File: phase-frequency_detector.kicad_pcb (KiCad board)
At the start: 2 copper layers, 160 x 100 mm, 89 parts, among them J1 REF, J2 IN, J3 Error_Out, J4 C64AC, J5 Switch, J6 Fast_Out, U1 HMC439QS16G, U2 LT3045EMSE, U3 LT3094EMSE, U4 ADA4896-2ARMZ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

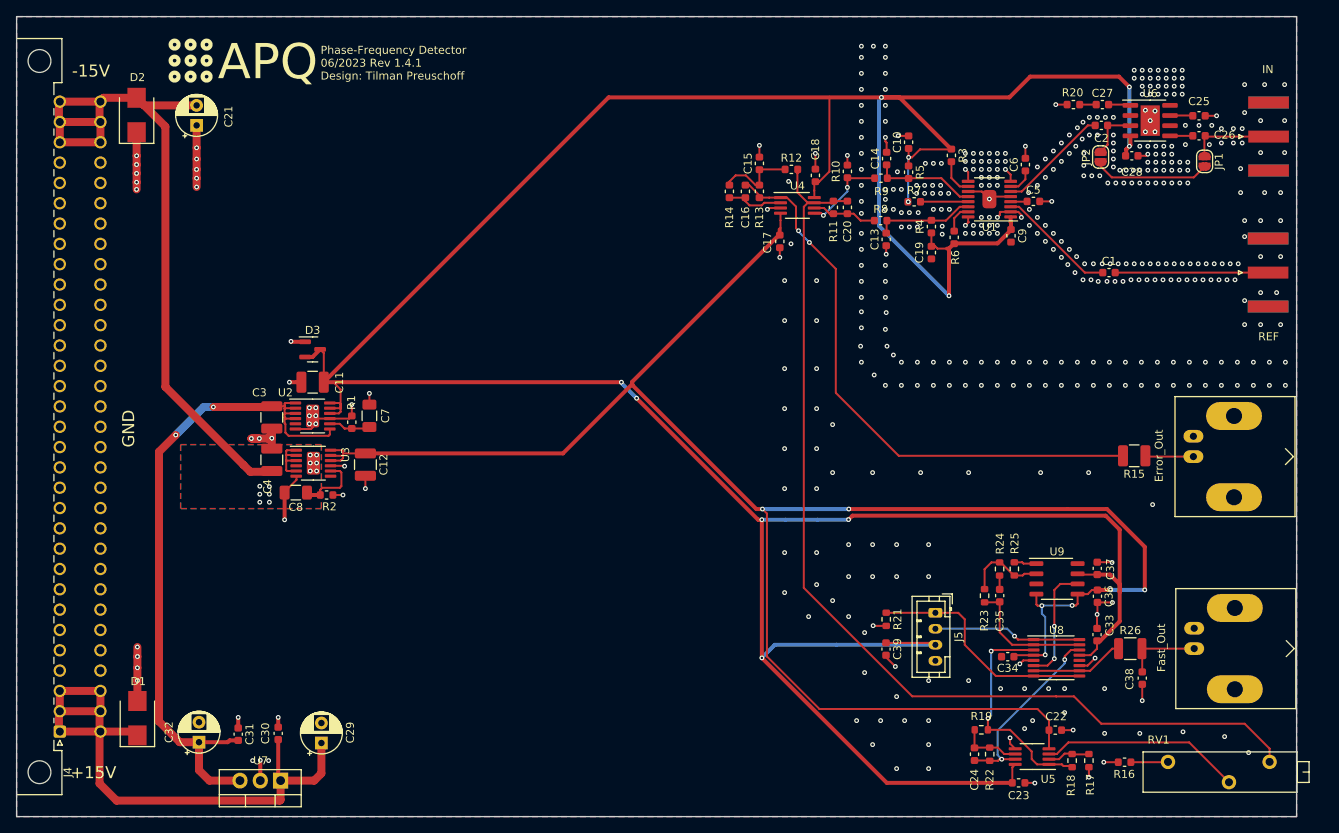
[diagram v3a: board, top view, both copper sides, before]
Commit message: Updated to KiCad 7 Added CI pipeline Fixed trailing whitespaces of MFN and PN labels Fixed ERC/DRC errors
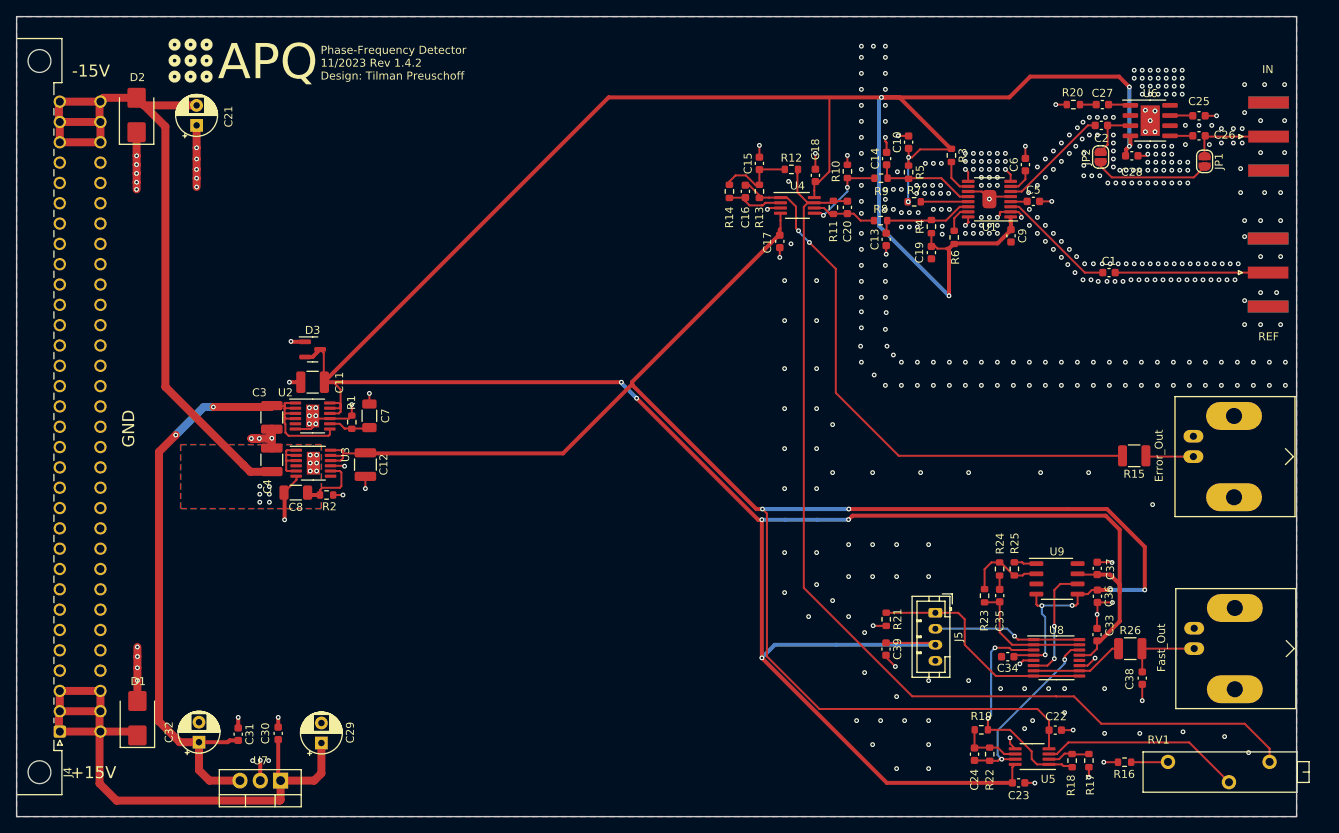
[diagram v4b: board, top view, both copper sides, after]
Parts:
- U6: footprint footprints:SOIC-8-1EP_3.9x4.9mm_P1.27mm_EP2.41x3.81mm_DNF -> Package_SO:SOIC-8-1EP_3.9x4.9mm_P1.27mm_EP2.41x3.81mm
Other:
- rule pad_to_mask_clearance: 0.2 -> 0
- board text added: "Phase-Frequency Detector 11/2023 Rev 1.4.2 Design: Tilman Preuschoff"
- board text removed: "Phase-Frequency Detector 06/2023 Rev 1.4.1 Design: Tilman Preuschoff"

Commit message: Update LT3045/LT3094 symbols
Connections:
- net IN renamed Net-(D2-A2)
